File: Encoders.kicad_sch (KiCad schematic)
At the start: 23 parts, among them J10 WHEEL_RIGHT, J8 STEERING_WHEEL, J9 WHEEL_LEFT, U3 MAX490E, U8 UA9637A, U9 UA9637A

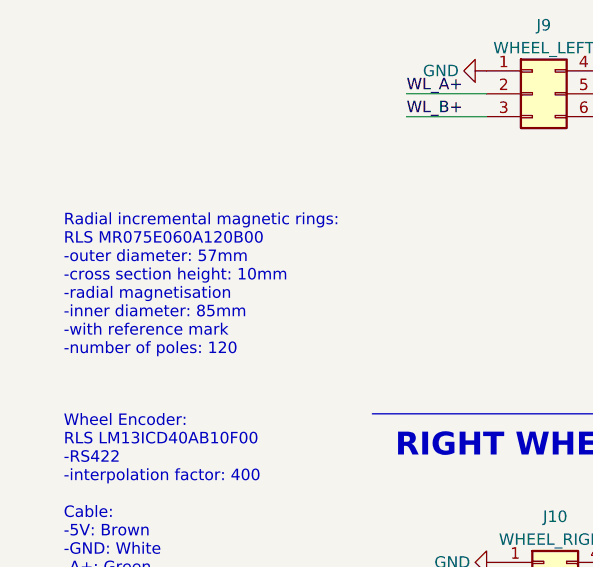
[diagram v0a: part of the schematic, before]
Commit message: fix wrong data on encoder
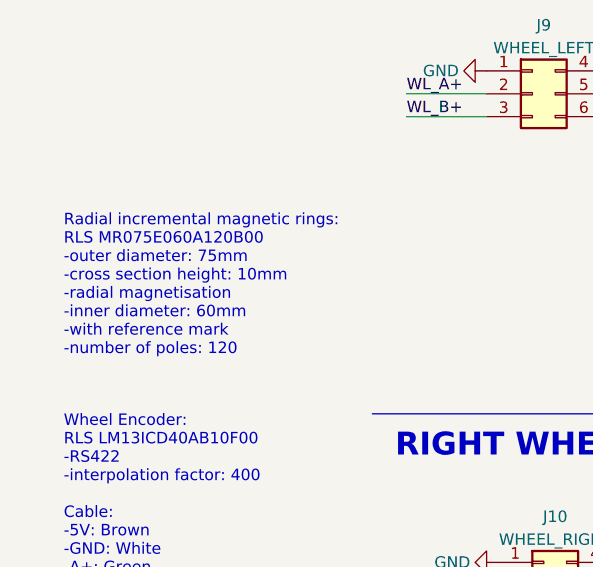
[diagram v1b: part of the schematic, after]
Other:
- note added: "Radial incremental magnetic rings: RLS MR075E060A120B00 -outer diameter: 75mm -cross section height: 10mm -radial magnetisation -inner diameter: 60mm -with reference mark -number of poles: 120"
- note removed: "Radial incremental magnetic rings: RLS MR075E060A120B00 -outer diameter: 57mm -cross section height: 10mm -radial magnetisation -inner diameter: 85mm -with reference mark -number of poles: 120"
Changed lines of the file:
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@@
     (effects (font (size 2.54 2.54) (thickness 0.508) bold) (justify left bottom))
   )
-  (text "Radial incremental magnetic rings: \nRLS MR075E060A120B00\n-outer diameter: 57mm\n-cross section height: 10mm\n-radial magnetisation\n-inner diameter: 85mm\n-with reference mark\n-number of poles: 120"
+  (text "Radial incremental magnetic rings: \nRLS MR075E060A120B00\n-outer diameter: 75mm\n-cross section height: 10mm\n-radial magnetisation\n-inner diameter: 60mm\n-with reference mark\n-number of poles: 120"
     (at 17.78 128.27 0)
     (effects (font (size 1.27 1.27)) (justify left bottom))
